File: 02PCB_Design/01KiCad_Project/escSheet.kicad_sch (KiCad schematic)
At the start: 1 part, among them J2 Screw_Terminal_01x03

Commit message: Layout progress
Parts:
- J2: footprint (none) -> TerminalBlock_Phoenix:TerminalBlock_Phoenix_MKDS-3-3-5.08_1x03_P5.08mm_Horizontal
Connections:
- net HalfBridgePowerStage1/PH_OUT: now also J2.3 (Pin_3); no longer J2.1 (Pin_1)
- net HalfBridgePowerStage3/PH_OUT: now also J2.1 (Pin_1); no longer J2.3 (Pin_3)
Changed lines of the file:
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@@
-    (stroke (width 0) (type default))
-  )
-  (wire (pts (xy 228.6 104.14) (xy 246.38 104.14))
-    (stroke (width 0) (type default))
-  )
-  (wire (pts (xy 228.6 144.78) (xy 228.6 109.22))
     (stroke (width 0) (type default))
   )
@@
     (stroke (width 0) (type default))
   )
+  (wire (pts (xy 212.09 106.68) (xy 194.31 106.68))
+    (stroke (width 0) (type default))
+  )
   (wire (pts (xy 82.55 142.24) (xy 95.25 142.24))
     (stroke (width 0) (type default))
@@
     (stroke (width 0) (type default))
   )
-  (wire (pts (xy 228.6 68.58) (xy 228.6 104.14))
+  (wire (pts (xy 215.9 106.68) (xy 246.38 106.68))
     (stroke (width 0) (type default))
   )
@@
     (stroke (width 0) (type default))
   )
-  (wire (pts (xy 194.31 144.78) (xy 228.6 144.78))
+  (wire (pts (xy 194.31 144.78) (xy 236.22 144.78))
     (stroke (width 0) (type default))
   )
@@
     (stroke (width 0) (type default))
   )
+  (wire (pts (xy 212.09 109.22) (xy 215.9 109.22))
+    (stroke (width 0) (type default))
+  )
   (wire (pts (xy 82.55 93.98) (xy 95.25 93.98))
+    (stroke (width 0) (type default))
+  )
+  (wire (pts (xy 212.09 109.22) (xy 212.09 106.68))
     (stroke (width 0) (type default))
   )
@@
     (stroke (width 0) (type default))
   )
+  (wire (pts (xy 246.38 104.14) (xy 236.22 104.14))
+    (stroke (width 0) (type default))
+  )
   (wire (pts (xy 134.62 102.87) (xy 171.45 102.87))
     (stroke (width 0) (type default))
   )
   (wire (pts (xy 95.25 33.02) (xy 78.74 33.02))
+    (stroke (width 0) (type default))
+  )
+  (wire (pts (xy 236.22 104.14) (xy 236.22 144.78))
     (stroke (width 0) (type default))
   )
@@
     (stroke (width 0) (type default))
   )
-  (wire (pts (xy 194.31 106.68) (xy 246.38 106.68))
+  (wire (pts (xy 228.6 68.58) (xy 228.6 109.22))
+    (stroke (width 0) (type default))
+  )
+  (wire (pts (xy 215.9 109.22) (xy 215.9 106.68))
     (stroke (width 0) (type default))
   )
@@
       (effects (font (size 1.27 1.27)) (justify left))
     )
-    (property "Footprint" "" (at 251.46 106.68 0)
+    (property "Footprint" "TerminalBlock_Phoenix:TerminalBlock_Phoenix_MKDS-3-3-5.08_1x03_P5.08mm_Horizontal" (at 251.46 106.68 0)
       (effects (font (size 1.27 1.27)) hide)
     )

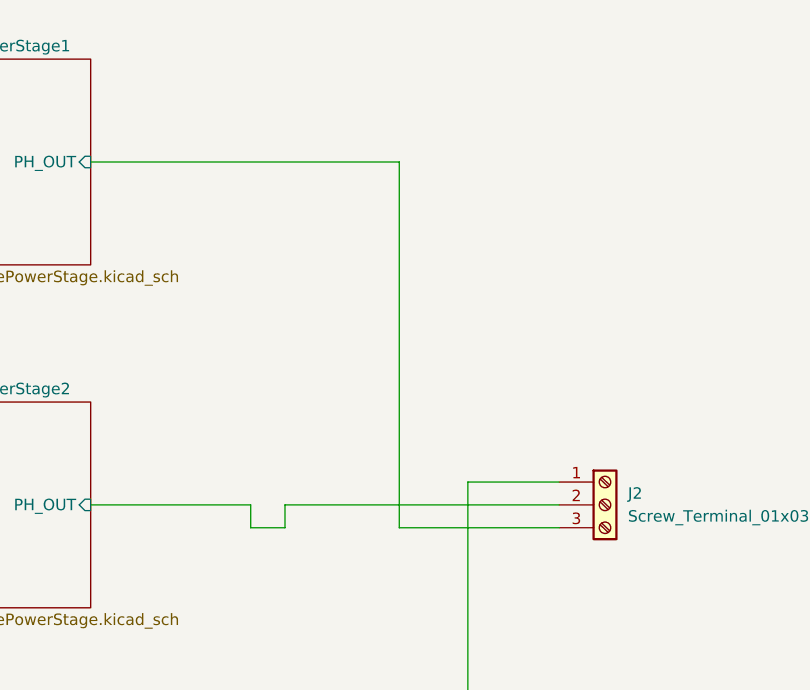
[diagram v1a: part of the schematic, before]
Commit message: routed signals
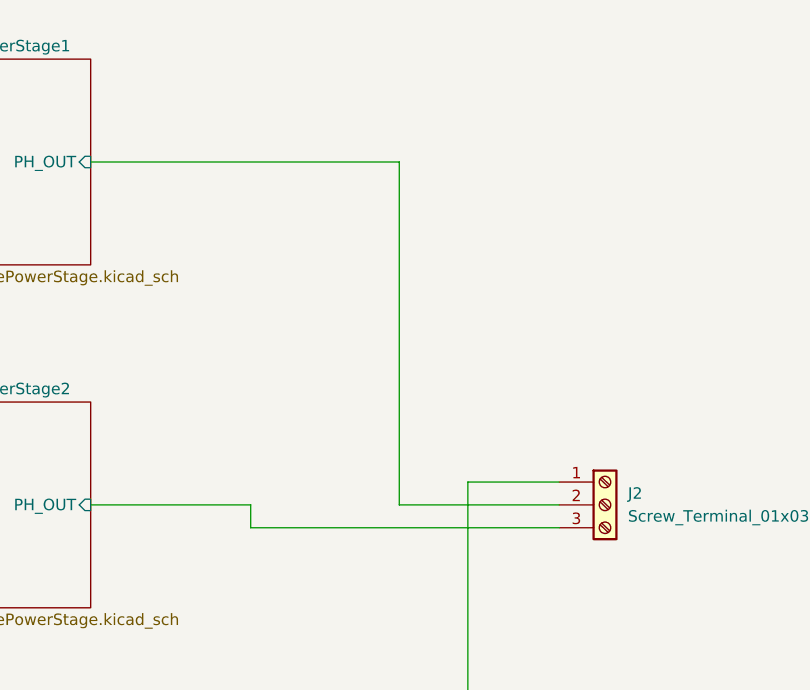
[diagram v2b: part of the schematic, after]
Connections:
- net HalfBridgePowerStage1/PH_OUT: now also J2.2 (Pin_2); no longer J2.3 (Pin_3)
- net HalfBridgePowerStage2/PH_OUT: now also J2.3 (Pin_3); no longer J2.2 (Pin_2)
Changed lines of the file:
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@@
-    (stroke (width 0) (type default))
-  )
-  (wire (pts (xy 215.9 106.68) (xy 246.38 106.68))
     (stroke (width 0) (type default))
   )
@@
     (stroke (width 0) (type default))
   )
-  (wire (pts (xy 228.6 109.22) (xy 246.38 109.22))
-    (stroke (width 0) (type default))
-  )
   (wire (pts (xy 82.55 110.49) (xy 95.25 110.49))
     (stroke (width 0) (type default))
@@
     (stroke (width 0) (type default))
   )
-  (wire (pts (xy 212.09 109.22) (xy 215.9 109.22))
+  (wire (pts (xy 212.09 109.22) (xy 246.38 109.22))
     (stroke (width 0) (type default))
   )
   (wire (pts (xy 82.55 93.98) (xy 95.25 93.98))
+    (stroke (width 0) (type default))
+  )
+  (wire (pts (xy 228.6 68.58) (xy 228.6 106.68))
     (stroke (width 0) (type default))
   )
@@
   )
   (wire (pts (xy 82.55 36.83) (xy 95.25 36.83))
+    (stroke (width 0) (type default))
+  )
+  (wire (pts (xy 228.6 106.68) (xy 246.38 106.68))
     (stroke (width 0) (type default))
   )
@@
     (stroke (width 0) (type default))
   )
-  (wire (pts (xy 228.6 68.58) (xy 228.6 109.22))
-    (stroke (width 0) (type default))
-  )
-  (wire (pts (xy 215.9 109.22) (xy 215.9 106.68))
-    (stroke (width 0) (type default))
-  )

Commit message: Design 1.0 Finished
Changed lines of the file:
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@@
-    (stroke (width 0) (type default))
-  )
-  (wire (pts (xy 212.09 106.68) (xy 194.31 106.68))
     (stroke (width 0) (type default))
   )
@@
     (stroke (width 0) (type default))
   )
-  (wire (pts (xy 212.09 109.22) (xy 246.38 109.22))
+  (wire (pts (xy 194.31 109.22) (xy 246.38 109.22))
     (stroke (width 0) (type default))
   )
@@
   )
   (wire (pts (xy 228.6 68.58) (xy 228.6 106.68))
-    (stroke (width 0) (type default))
-  )
-  (wire (pts (xy 212.09 109.22) (xy 212.09 106.68))
     (stroke (width 0) (type default))
   )
@@
       (effects (font (size 1.27 1.27)) (justify left top))
     )
-    (pin "PH_OUT" input (at 194.31 106.68 0)
-      (effects (font (size 1.27 1.27)) (justify right))
-    )
+    (pin "PH_OUT" input (at 194.31 109.22 0)
+      (effects (font (size 1.27 1.27)) (justify right))
+    )
